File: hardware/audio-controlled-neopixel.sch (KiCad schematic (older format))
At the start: 64 parts, among them J1 AudioJack4, J2 AudioJack4, J3 KF2EDGK, J4 KF2EDGK, J5 KF2EDGK, J6 Conn_01x01_Female, J7 Conn_01x01_Female, J8 Conn_01x01_Female, J9 Conn_01x01_Female, SW1 SW_SPST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

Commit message: adjusted component values for better real world performance, changed diode types, minor PCB changes for better ground return paths
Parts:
- removed D7, D8, D9: 1N5819, Diode_SMD:D_SOD-123, symbol Diode:BAT85
- added D1, D3, D7: BAT20JFILM, Diode_SMD:D_SOD-323, symbol Diode:1N4148
- D4, D5, D6: value 1N4148 -> BAT20JFILM; footprint Diode_SMD:D_SOD-123 -> Diode_SMD:D_SOD-323
- R21, R23: value 100K -> 0R
- R22: value 250K -> NF
- R24: value 169K -> NF
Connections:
- net +5V: now also D1.1 (K), D3.1 (K), D7.1 (K)
- net High: now also D7.2 (A)
- net Low: now also D1.2 (A)
- net Mid: now also D3.2 (A)
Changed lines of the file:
@@
 	7425 975  7500 975
-$Comp
-L Diode:BAT85 D7
-U 1 1 5BF7321B
-P 7375 2475
-F 0 "D7" V 7329 2554 50  0000 L CNN
-F 1 "1N5819" V 7420 2554 50  0000 L CNN
-F 2 "Diode_SMD:D_SOD-123" H 7375 2300 50  0001 C CNN
-F 3 "http://www.nxp.com/documents/data_sheet/BAT85.pdf" H 7375 2475 50  0001 C CNN
-	1    7375 2475
-	0    1    1    0
-$EndComp
-$Comp
-L Diode:BAT85 D8
-U 1 1 5BF7345F
-P 7375 3575
-F 0 "D8" V 7329 3654 50  0000 L CNN
-F 1 "1N5819" V 7420 3654 50  0000 L CNN
-F 2 "Diode_SMD:D_SOD-123" H 7375 3400 50  0001 C CNN
-F 3 "http://www.nxp.com/documents/data_sheet/BAT85.pdf" H 7375 3575 50  0001 C CNN
-	1    7375 3575
-	0    1    1    0
-$EndComp
-$Comp
-L Diode:BAT85 D9
-U 1 1 5BF737DB
-P 7375 4825
-F 0 "D9" V 7329 4904 50  0000 L CNN
-F 1 "1N5819" V 7420 4904 50  0000 L CNN
-F 2 "Diode_SMD:D_SOD-123" H 7375 4650 50  0001 C CNN
-F 3 "http://www.nxp.com/documents/data_sheet/BAT85.pdf" H 7375 4825 50  0001 C CNN
-	1    7375 4825
-	0    1    1    0
-$EndComp
 $Comp
 L Connector:Conn_01x03_Female J4
@@
 P 6725 2675
 F 0 "D4" H 6725 2459 50  0000 C CNN
-F 1 "1N4148" H 6725 2550 50  0000 C CNN
-F 2 "Diode_SMD:D_SOD-123" H 6725 2500 50  0001 C CNN
+F 1 "BAT20JFILM" H 6725 2550 50  0000 C CNN
+F 2 "Diode_SMD:D_SOD-323" H 6725 2500 50  0001 C CNN
 F 3 "http://www.nxp.com/documents/data_sheet/1N4148_1N4448.pdf" H 6725 2675 50  0001 C CNN
 	1    6725 2675
@@
 P 6725 3775
 F 0 "D5" H 6725 3559 50  0000 C CNN
-F 1 "1N4148" H 6725 3650 50  0000 C CNN
-F 2 "Diode_SMD:D_SOD-123" H 6725 3600 50  0001 C CNN
+F 1 "BAT20JFILM" H 6725 3650 50  0000 C CNN
+F 2 "Diode_SMD:D_SOD-323" H 6725 3600 50  0001 C CNN
 F 3 "http://www.nxp.com/documents/data_sheet/1N4148_1N4448.pdf" H 6725 3775 50  0001 C CNN
 	1    6725 3775
@@
 P 6725 5050
 F 0 "D6" H 6725 4834 50  0000 C CNN
-F 1 "1N4148" H 6725 4925 50  0000 C CNN
-F 2 "Diode_SMD:D_SOD-123" H 6725 4875 50  0001 C CNN
+F 1 "BAT20JFILM" H 6725 4925 50  0000 C CNN
+F 2 "Diode_SMD:D_SOD-323" H 6725 4875 50  0001 C CNN
 F 3 "http://www.nxp.com/documents/data_sheet/1N4148_1N4448.pdf" H 6725 5050 50  0001 C CNN
 	1    6725 5050
@@
 P 4925 3525
 F 0 "R23" H 5000 3550 50  0000 L CNN
-F 1 "100K" H 5000 3475 50  0000 L CNN
+F 1 "0R" H 5000 3475 50  0000 L CNN
 F 2 "Resistor_SMD:R_0805_2012Metric" H 4925 3525 50  0001 C CNN
 F 3 "~" H 4925 3525 50  0001 C CNN
@@
 P 4925 3825
 F 0 "R24" H 5000 3850 50  0000 L CNN
-F 1 "169K" H 5000 3775 50  0000 L CNN
+F 1 "NF" H 5000 3775 50  0000 L CNN
 F 2 "Resistor_SMD:R_0805_2012Metric" H 4925 3825 50  0001 C CNN
 F 3 "~" H 4925 3825 50  0001 C CNN
@@
 P 4900 2425
 F 0 "R21" H 4975 2450 50  0000 L CNN
-F 1 "100K" H 4975 2375 50  0000 L CNN
+F 1 "0R" H 4975 2375 50  0000 L CNN
 F 2 "Resistor_SMD:R_0805_2012Metric" H 4900 2425 50  0001 C CNN
 F 3 "~" H 4900 2425 50  0001 C CNN
@@
 P 4900 2725
 F 0 "R22" H 4975 2750 50  0000 L CNN
-F 1 "250K" H 4975 2675 50  0000 L CNN
+F 1 "NF" H 4975 2675 50  0000 L CNN
 F 2 "Resistor_SMD:R_0805_2012Metric" H 4900 2725 50  0001 C CNN
 F 3 "~" H 4900 2725 50  0001 C CNN
@@
 Wire Wire Line
 	10375 4875 10375 4925
+$Comp
+L Diode:1N4148 D1
+U 1 1 5C7FB734
+P 7375 2475
+F 0 "D1" H 7375 2259 50  0000 C CNN
+F 1 "BAT20JFILM" H 7375 2350 50  0000 C CNN
+F 2 "Diode_SMD:D_SOD-323" H 7375 2300 50  0001 C CNN
+F 3 "http://www.nxp.com/documents/data_sheet/1N4148_1N4448.pdf" H 7375 2475 50  0001 C CNN
+	1    7375 2475
+	0    1    1    0
+$EndComp
+$Comp
+L Diode:1N4148 D3
+U 1 1 5C81F5DF
+P 7375 3575
+F 0 "D3" H 7375 3359 50  0000 C CNN
+F 1 "BAT20JFILM" H 7375 3450 50  0000 C CNN
+F 2 "Diode_SMD:D_SOD-323" H 7375 3400 50  0001 C CNN
+F 3 "http://www.nxp.com/documents/data_sheet/1N4148_1N4448.pdf" H 7375 3575 50  0001 C CNN
+	1    7375 3575
+	0    1    1    0
+$EndComp
+$Comp
+L Diode:1N4148 D7
+U 1 1 5C81F693
+P 7375 4825
+F 0 "D7" H 7375 4609 50  0000 C CNN
+F 1 "BAT20JFILM" H 7375 4700 50  0000 C CNN
+F 2 "Diode_SMD:D_SOD-323" H 7375 4650 50  0001 C CNN
+F 3 "http://www.nxp.com/documents/data_sheet/1N4148_1N4448.pdf" H 7375 4825 50  0001 C CNN
+	1    7375 4825
+	0    1    1    0
+$EndComp
 $EndSCHEMATC

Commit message: hardware updates
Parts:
- removed C2: 10u, Capacitor_THT:CP_Radial_D5.0mm_P2.00mm, symbol Device:CP_Small
- removed R17: 10K, Resistor_SMD:R_0805_2012Metric, symbol Device:R_Small
- removed R21, R23, R25: 0R, Resistor_SMD:R_0805_2012Metric, symbol Device:R_Small
- removed R22, R24, R26: NF, Resistor_SMD:R_0805_2012Metric, symbol Device:R_Small
- removed RV1: 10KA, Potentiometer_THT:Potentiometer_Alps_RK097_Dual_Horizontal, symbol Device:R_POT_Dual_Separate
- removed U1: LM324, Package_SO:SOIC-14_3.9x8.7mm_P1.27mm, symbol Amplifier_Operational:LM324
- added J10: Conn_01x04_Male, Connector_PinHeader_2.54mm:PinHeader_1x04_P2.54mm_Vertical, symbol Connector:Conn_01x04_Male
- added R19: 10K, Resistor_SMD:R_0805_2012Metric, symbol Device:R_Small
- added R20: 200K, Resistor_SMD:R_0805_2012Metric, symbol Device:R_Small
- added RV1: R_POT, Potentiometer_THT:Potentiometer_Alps_RK097_Single_Horizontal, symbol Device:R_POT
- added RV2, RV3, RV4: 5K, Potentiometer_SMD:Potentiometer_Vishay_TS53YJ_Vertical, symbol Device:R_POT
- added U1: LM358, Package_SO:SOIC-8_3.9x4.9mm_P1.27mm, symbol Amplifier_Operational:LM358
- C19: footprint Capacitor_THT:CP_Radial_D10.0mm_P5.00mm -> Capacitor_SMD:CP_Elec_10x10
- J1, J2: footprint Connector_Audio:Jack_3.5mm_PJ320D_Horizontal -> custom:Jack_3.5mm_PJ320D_Horizontal
- R5: value 200K -> 10K
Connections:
- net +12V: now also J10.4 (Pin_4), U1.4 (V-)
- net +5V: now also J10.1 (Pin_1); no longer A1.27 (+5V), SW1.1 (A)
- net -12V: now also U1.8 (V+)
- net GND: now also R6.2, SW1.1 (A), R19.2, RV1.1, RV2.3, RV3.3, RV4.3; no longer R6.1
- net Input_L: now also R3.2, R6.1; no longer R6.2
- net Input_R: now also R2.1
- net at C6.2: now also RV4.2
- net at C5.2: now also RV3.2
- net at R2.2, R3.1, R5.2: now also U1.2 (-)
- net at R5.1: now also C1.2, U1.1
- net at C4.2: now also RV2.2
- net at R4.1: now also U1.3 (+)
- net at A1.30 (VIN): now also J10.3 (Pin_3)
- net at C1.1: now also RV1.3
- new net: A1.27 (+5V), J10.2 (Pin_2)
- new net: RV1.2, U1.5 (+)
- new net: R19.1, R20.2, U1.6 (-)
- new net: R20.1, RV2.1, RV3.1, RV4.1, U1.7
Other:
- moved on the sheet: A1, C1, C10, C11, C12, C13, C14, C15, C3, C4, C5, C6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

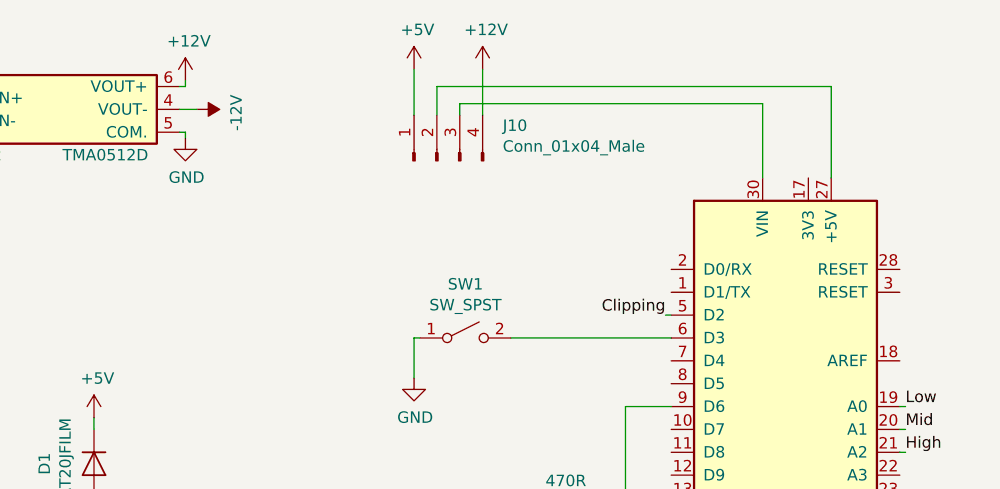
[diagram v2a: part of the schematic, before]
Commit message: added power supply filtering
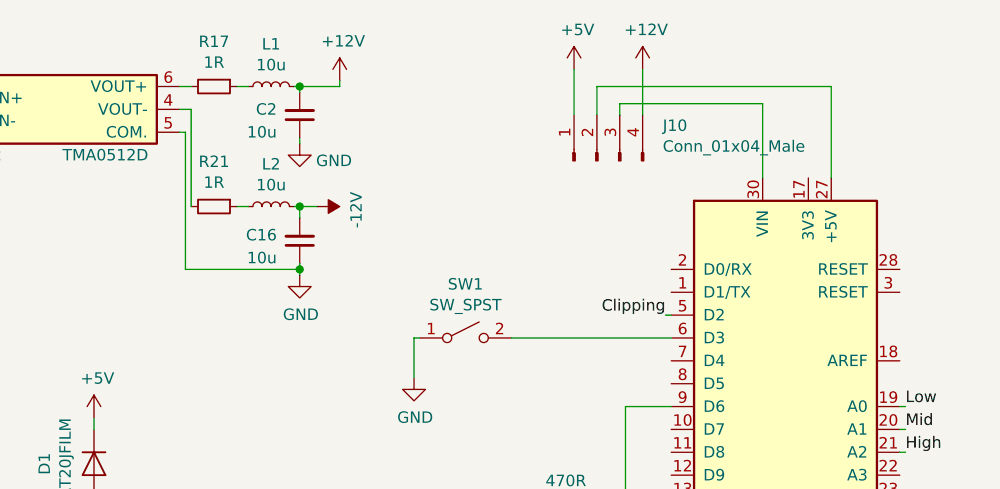
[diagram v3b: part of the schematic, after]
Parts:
- added C16, C2: 10u, Capacitor_SMD:C_0805_2012Metric, symbol Device:C_Small
- added L1, L2: 10u, Inductor_SMD:L_0805_2012Metric, symbol Device:L_Small
- added R17, R21: 1R, Resistor_SMD:R_0805_2012Metric, symbol Device:R_Small
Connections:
- net +12V: now also C2.2, L1.2; no longer U2.6 (VOUT+)
- net -12V: now also C16.2, L2.2; no longer U2.4 (VOUT-)
- net GND: now also C16.1, C2.1
- new net: R21.2, U2.4 (VOUT-)
- new net: R17.2, U2.6 (VOUT+)
- new net: L1.1, R17.1
- new net: L2.1, R21.1
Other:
- moved on the sheet: J10
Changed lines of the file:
@@
 L power:+12V #PWR0106
 U 1 1 5BF24254
-P 7450 850
-F 0 "#PWR0106" H 7450 700 50  0001 C CNN
-F 1 "+12V" H 7465 1023 50  0000 C CNN
-F 2 "" H 7450 850 50  0001 C CNN
-F 3 "" H 7450 850 50  0001 C CNN
-	1    7450 850
+P 8125 850
+F 0 "#PWR0106" H 8125 700 50  0001 C CNN
+F 1 "+12V" H 8140 1023 50  0000 C CNN
+F 2 "" H 8125 850 50  0001 C CNN
+F 3 "" H 8125 850 50  0001 C CNN
+	1    8125 850
 	1    0    0    -1
 $EndComp
@@
 L power:-12V #PWR0107
 U 1 1 5BF242D9
-P 7500 975
-F 0 "#PWR0107" H 7500 1075 50  0001 C CNN
-F 1 "-12V" H 7515 1148 50  0000 C CNN
-F 2 "" H 7500 975 50  0001 C CNN
-F 3 "" H 7500 975 50  0001 C CNN
-	1    7500 975
+P 8025 1400
+F 0 "#PWR0107" H 8025 1500 50  0001 C CNN
+F 1 "-12V" H 8040 1573 50  0000 C CNN
+F 2 "" H 8025 1400 50  0001 C CNN
+F 3 "" H 8025 1400 50  0001 C CNN
+	1    8025 1400
 	0    1    1    0
 $EndComp
 Wire Wire Line
-	7450 1100 7450 1075
-Wire Wire Line
-	7450 1075 7425 1075
-Wire Wire Line
-	7450 850  7450 875
-Wire Wire Line
-	7450 875  7425 875
-Wire Wire Line
-	7425 975  7500 975
+	8125 850  8125 875
+Wire Wire Line
+	7950 1400 8025 1400
 $Comp
 L Connector:Conn_01x03_Female J4
@@
 L power:GND #PWR0111
 U 1 1 5C0E2BC2
-P 7450 1100
-F 0 "#PWR0111" H 7450 850 50  0001 C CNN
-F 1 "GND" H 7455 927 50  0000 C CNN
-F 2 "" H 7450 1100 50  0001 C CNN
-F 3 "" H 7450 1100 50  0001 C CNN
-	1    7450 1100
+P 7950 1700
+F 0 "#PWR0111" H 7950 1450 50  0001 C CNN
+F 1 "GND" H 7955 1527 50  0000 C CNN
+F 2 "" H 7950 1700 50  0001 C CNN
+F 3 "" H 7950 1700 50  0001 C CNN
+	1    7950 1700
 	1    0    0    -1
 $EndComp
@@
 	8875 1975 9575 1975
 Wire Wire Line
-	8750 800  8750 1000
+	9450 800  9450 1000
 $Comp
 L power:+12V #PWR0116
 U 1 1 5CFEA3EA
-P 8750 800
-F 0 "#PWR0116" H 8750 650 50  0001 C CNN
-F 1 "+12V" H 8765 973 50  0000 C CNN
-F 2 "" H 8750 800 50  0001 C CNN
-F 3 "" H 8750 800 50  0001 C CNN
-	1    8750 800
+P 9450 800
+F 0 "#PWR0116" H 9450 650 50  0001 C CNN
+F 1 "+12V" H 9465 973 50  0000 C CNN
+F 2 "" H 9450 800 50  0001 C CNN
+F 3 "" H 9450 800 50  0001 C CNN
+	1    9450 800
 	1    0    0    -1
 $EndComp
@@
 	9975 950  9975 1275
 Wire Wire Line
-	8650 1000 8650 950
+	9350 1000 9350 950
 $Comp
 L Connector:Conn_01x04_Male J10
 U 1 1 5CF82519
-P 8550 1200
-F 0 "J10" V 8704 912 50  0000 R CNN
-F 1 "Conn_01x04_Male" V 8613 912 50  0000 R CNN
-F 2 "Connector_PinHeader_2.54mm:PinHeader_1x04_P2.54mm_Vertical" H 8550 1200 50  0001 C CNN
-F 3 "~" H 8550 1200 50  0001 C CNN
-	1    8550 1200
+P 9250 1200
+F 0 "J10" V 9404 912 50  0000 R CNN
+F 1 "Conn_01x04_Male" V 9313 912 50  0000 R CNN
+F 2 "Connector_PinHeader_2.54mm:PinHeader_1x04_P2.54mm_Vertical" H 9250 1200 50  0001 C CNN
+F 3 "~" H 9250 1200 50  0001 C CNN
+	1    9250 1200
 	0    -1   -1   0
 $EndComp
@@
 L power:+5V #PWR0120
 U 1 1 5C1551B0
-P 8450 800
-F 0 "#PWR0120" H 8450 650 50  0001 C CNN
-F 1 "+5V" H 8465 973 50  0000 C CNN
-F 2 "" H 8450 800 50  0001 C CNN
-F 3 "" H 8450 800 50  0001 C CNN
-	1    8450 800
-	1    0    0    -1
-$EndComp
-Wire Wire Line
-	8450 800  8450 1000
-Wire Wire Line
-	8650 950  9975 950
-Wire Wire Line
-	8550 1000 8550 875
-Wire Wire Line
-	8550 875  10275 875
+P 9150 800
+F 0 "#PWR0120" H 9150 650 50  0001 C CNN
+F 1 "+5V" H 9165 973 50  0000 C CNN
+F 2 "" H 9150 800 50  0001 C CNN
+F 3 "" H 9150 800 50  0001 C CNN
+	1    9150 800
+	1    0    0    -1
+$EndComp
+Wire Wire Line
+	9150 800  9150 1000
+Wire Wire Line
+	9250 1000 9250 875
 Wire Wire Line
 	10275 875  10275 1275
@@
 Wire Wire Line
 	10625 2775 10575 2775
+$Comp
+L Device:R_Small R17
+U 1 1 5D33B017
+P 7575 875
+F 0 "R17" V 7379 875 50  0000 C CNN
+F 1 "1R" V 7470 875 50  0000 C CNN
+F 2 "Resistor_SMD:R_0805_2012Metric" H 7575 875 50  0001 C CNN
+F 3 "~" H 7575 875 50  0001 C CNN
+	1    7575 875
+	0    1    1    0
+$EndComp
+$Comp
+L Device:R_Small R21
+U 1 1 5D33B62F
+P 7575 1400
+F 0 "R21" V 7379 1400 50  0000 C CNN
+F 1 "1R" V 7470 1400 50  0000 C CNN
+F 2 "Resistor_SMD:R_0805_2012Metric" H 7575 1400 50  0001 C CNN
+F 3 "~" H 7575 1400 50  0001 C CNN
+	1    7575 1400
+	0    1    1    0
+$EndComp
+$Comp
+L Device:L_Small L1
+U 1 1 5D33C39C
+P 7825 875
+F 0 "L1" V 8010 875 50  0000 C CNN
+F 1 "10u" V 7919 875 50  0000 C CNN
+F 2 "Inductor_SMD:L_0805_2012Metric" H 7825 875 50  0001 C CNN
+F 3 "~" H 7825 875 50  0001 C CNN
+	1    7825 875
+	0    -1   -1   0
+$EndComp
+Wire Wire Line
+	9975 950  9350 950
+Wire Wire Line
+	9250 875  10275 875
+$Comp
+L Device:C_Small C2
+U 1 1 5D37B523
+P 7950 1000
+F 0 "C2" H 7850 975 50  0000 R CNN
+F 1 "10u" H 7850 1075 50  0000 R CNN
+F 2 "Capacitor_SMD:C_0805_2012Metric" H 7950 1000 50  0001 C CNN
+F 3 "~" H 7950 1000 50  0001 C CNN
+	1    7950 1000
+	1    0    0    1
+$EndComp
+$Comp
+L Device:L_Small L2
+U 1 1 5D38C072
+P 7825 1400
+F 0 "L2" V 8010 1400 50  0000 C CNN
+F 1 "10u" V 7919 1400 50  0000 C CNN
+F 2 "Inductor_SMD:L_0805_2012Metric" H 7825 1400 50  0001 C CNN
+F 3 "~" H 7825 1400 50  0001 C CNN
+	1    7825 1400
+	0    -1   -1   0
+$EndComp
+$Comp
+L Device:C_Small C16
+U 1 1 5D38C370
+P 7950 1550
+F 0 "C16" H 7850 1525 50  0000 R CNN
+F 1 "10u" H 7850 1625 50  0000 R CNN
+F 2 "Capacitor_SMD:C_0805_2012Metric" H 7950 1550 50  0001 C CNN
+F 3 "~" H 7950 1550 50  0001 C CNN
+	1    7950 1550
+	1    0    0    1
+$EndComp
+Wire Wire Line
+	7450 1075 7425 1075
+Wire Wire Line
+	7450 1675 7950 1675
+Wire Wire Line
+	7475 975  7425 975
+Wire Wire Line
+	7675 1400 7725 1400
+Wire Wire Line
+	7950 1450 7950 1400
+Wire Wire Line
+	7950 1400 7925 1400
+Wire Wire Line
+	7950 1650 7950 1675
+$Comp
+L power:GND #PWR0119
+U 1 1 5D3FFD52
+P 7950 1125
+F 0 "#PWR0119" H 7950 875 50  0001 C CNN
+F 1 "GND" H 8100 1050 50  0000 C CNN
+F 2 "" H 7950 1125 50  0001 C CNN
+F 3 "" H 7950 1125 50  0001 C CNN
+	1    7950 1125
+	1    0    0    -1
+$EndComp
+Wire Wire Line
+	7475 975  7475 1400
+Wire Wire Line
+	7450 1075 7450 1675
+Wire Wire Line
+	7950 1700 7950 1675
+Connection ~ 7950 1675
+Connection ~ 7950 1400
+Wire Wire Line
+	7425 875  7475 875
+Wire Wire Line
+	7675 875  7725 875
+Wire Wire Line
+	7925 875  7950 875
+Wire Wire Line
+	7950 900  7950 875
+Connection ~ 7950 875
+Wire Wire Line
+	7950 875  8125 875
+Wire Wire Line
+	7950 1125 7950 1100
 $EndSCHEMATC
